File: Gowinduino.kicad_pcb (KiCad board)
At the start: 2 copper layers, 68.6 x 53.3 mm, 63 parts, among them J1 Power, J2 Analog, J3 Digital, J4 Digital, J5 SPI, J6 JTAG, J7 USB, J8 12V, SW1 Mode, SW2 Reset, U1 GW1NSR-4CQN48P, U2 W25Q32JVSS, U3 TXB0104PW, U4 MP2122, U5 FT2232HL, U6 93LC56B, U7 XC6206-3.3, U8 L7805, Y1 12M

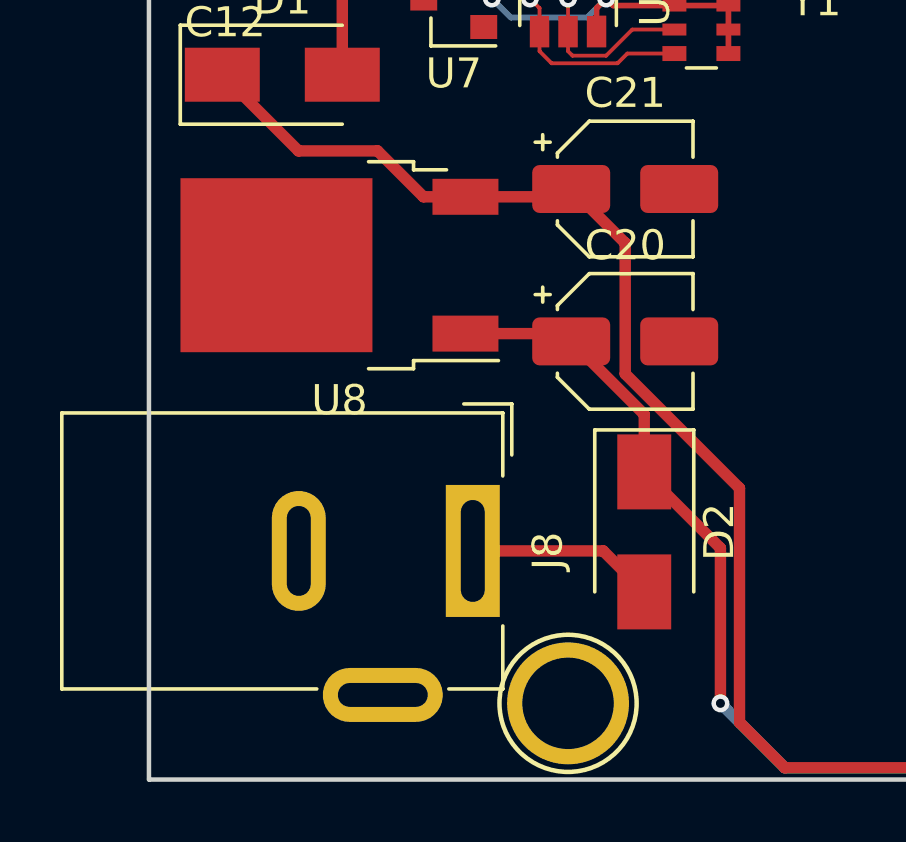
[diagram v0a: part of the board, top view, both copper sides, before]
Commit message: Via stitching at 5V regulator
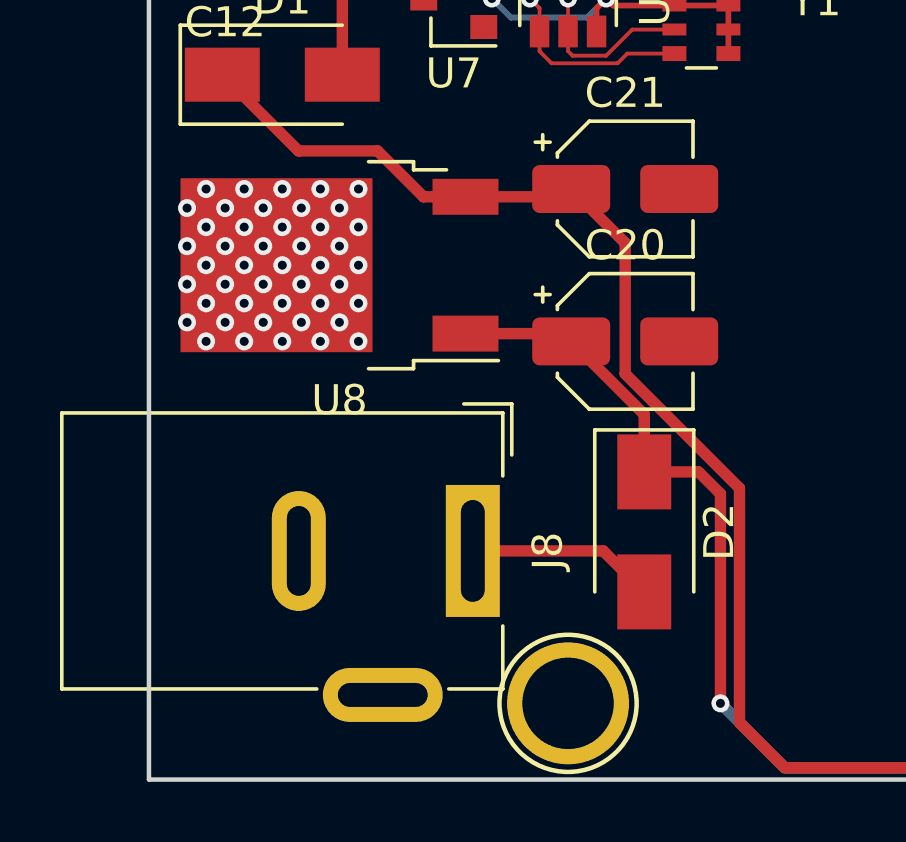
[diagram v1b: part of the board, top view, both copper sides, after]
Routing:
- net +12V: track 46.2 -> 47.3 mm
- net GND: vias 130 -> 175
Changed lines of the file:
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@@
     (thickness 1.6)
     (drawings 53)
-    (tracks 837)
+    (tracks 883)
     (zones 0)
     (modules 63)
@@
   (segment (start 151.454243 97.611827) (end 151.196056 97.35364) (width 0.127) (layer F.Cu) (net 0) (status 30))
   (segment (start 151.737086 97.328984) (end 151.478899 97.070797) (width 0.127) (layer F.Cu) (net 0) (status 30))
+  (via (at 117.983 111.76) (size 0.6) (drill 0.3) (layers F.Cu B.Cu) (net 2))
+  (via (at 117.983 106.68) (size 0.6) (drill 0.3) (layers F.Cu B.Cu) (net 2))
+  (via (at 112.903 111.76) (size 0.6) (drill 0.3) (layers F.Cu B.Cu) (net 2))
+  (via (at 112.268 111.125) (size 0.6) (drill 0.3) (layers F.Cu B.Cu) (net 2))
+  (via (at 116.713 106.68) (size 0.6) (drill 0.3) (layers F.Cu B.Cu) (net 2))
+  (via (at 117.348 107.315) (size 0.6) (drill 0.3) (layers F.Cu B.Cu) (net 2))
+  (via (at 117.983 107.95) (size 0.6) (drill 0.3) (layers F.Cu B.Cu) (net 2))
+  (via (at 116.078 109.855) (size 0.6) (drill 0.3) (layers F.Cu B.Cu) (net 2))
+  (via (at 114.173 111.76) (size 0.6) (drill 0.3) (layers F.Cu B.Cu) (net 2))
+  (via (at 113.538 111.125) (size 0.6) (drill 0.3) (layers F.Cu B.Cu) (net 2))
+  (via (at 112.903 110.49) (size 0.6) (drill 0.3) (layers F.Cu B.Cu) (net 2))
+  (via (at 112.268 109.855) (size 0.6) (drill 0.3) (layers F.Cu B.Cu) (net 2))
+  (via (at 115.443 106.68) (size 0.6) (drill 0.3) (layers F.Cu B.Cu) (net 2))
+  (via (at 116.078 107.315) (size 0.6) (drill 0.3) (layers F.Cu B.Cu) (net 2))
+  (via (at 116.713 107.95) (size 0.6) (drill 0.3) (layers F.Cu B.Cu) (net 2))
+  (via (at 117.348 108.585) (size 0.6) (drill 0.3) (layers F.Cu B.Cu) (net 2))
+  (via (at 117.983 109.22) (size 0.6) (drill 0.3) (layers F.Cu B.Cu) (net 2))
+  (via (at 116.713 110.49) (size 0.6) (drill 0.3) (layers F.Cu B.Cu) (net 2))
+  (via (at 115.443 111.76) (size 0.6) (drill 0.3) (layers F.Cu B.Cu) (net 2))
+  (via (at 114.808 111.125) (size 0.6) (drill 0.3) (layers F.Cu B.Cu) (net 2))
+  (via (at 114.173 110.49) (size 0.6) (drill 0.3) (layers F.Cu B.Cu) (net 2))
+  (via (at 113.538 109.855) (size 0.6) (drill 0.3) (layers F.Cu B.Cu) (net 2))
+  (via (at 112.903 109.22) (size 0.6) (drill 0.3) (layers F.Cu B.Cu) (net 2))
+  (via (at 112.268 108.585) (size 0.6) (drill 0.3) (layers F.Cu B.Cu) (net 2))
+  (via (at 114.173 106.68) (size 0.6) (drill 0.3) (layers F.Cu B.Cu) (net 2))
+  (via (at 114.808 107.315) (size 0.6) (drill 0.3) (layers F.Cu B.Cu) (net 2))
+  (via (at 115.443 107.95) (size 0.6) (drill 0.3) (layers F.Cu B.Cu) (net 2))
+  (via (at 116.078 108.585) (size 0.6) (drill 0.3) (layers F.Cu B.Cu) (net 2))
+  (via (at 116.713 109.22) (size 0.6) (drill 0.3) (layers F.Cu B.Cu) (net 2))
+  (via (at 117.348 109.855) (size 0.6) (drill 0.3) (layers F.Cu B.Cu) (net 2))
+  (via (at 117.983 110.49) (size 0.6) (drill 0.3) (layers F.Cu B.Cu) (net 2))
+  (via (at 117.348 111.125) (size 0.6) (drill 0.3) (layers F.Cu B.Cu) (net 2))
+  (via (at 116.713 111.76) (size 0.6) (drill 0.3) (layers F.Cu B.Cu) (net 2))
+  (via (at 116.078 111.125) (size 0.6) (drill 0.3) (layers F.Cu B.Cu) (net 2))
+  (via (at 115.443 110.49) (size 0.6) (drill 0.3) (layers F.Cu B.Cu) (net 2))
+  (via (at 114.808 109.855) (size 0.6) (drill 0.3) (layers F.Cu B.Cu) (net 2))
+  (via (at 114.173 109.22) (size 0.6) (drill 0.3) (layers F.Cu B.Cu) (net 2))
+  (via (at 113.538 108.585) (size 0.6) (drill 0.3) (layers F.Cu B.Cu) (net 2))
+  (via (at 112.903 107.95) (size 0.6) (drill 0.3) (layers F.Cu B.Cu) (net 2))
+  (via (at 112.268 107.315) (size 0.6) (drill 0.3) (layers F.Cu B.Cu) (net 2))
+  (via (at 112.903 106.68) (size 0.6) (drill 0.3) (layers F.Cu B.Cu) (net 2))
+  (via (at 113.538 107.315) (size 0.6) (drill 0.3) (layers F.Cu B.Cu) (net 2))
+  (via (at 114.173 107.95) (size 0.6) (drill 0.3) (layers F.Cu B.Cu) (net 2))
+  (via (at 114.808 108.585) (size 0.6) (drill 0.3) (layers F.Cu B.Cu) (net 2))
+  (via (at 115.443 109.22) (size 0.6) (drill 0.3) (layers F.Cu B.Cu) (net 2))
   (segment (start 177.038 95.885) (end 179.28074 98.12774) (width 0.1905) (layer B.Cu) (net 1))
   (segment (start 179.28074 113.165968) (end 174.498 117.948708) (width 0.1905) (layer B.Cu) (net 1))
@@
   (segment (start 132.19549 125.97249) (end 130.048 123.825) (width 0.381) (layer B.Cu) (net 42))
   (segment (start 154.57051 125.97249) (end 132.19549 125.97249) (width 0.381) (layer B.Cu) (net 42))
-  (segment (start 130.048 118.65) (end 127.508 116.11) (width 0.381) (layer F.Cu) (net 42))
-  (segment (start 130.048 123.825) (end 130.048 118.65) (width 0.381) (layer F.Cu) (net 42))
+  (segment (start 129.318 116.11) (end 127.508 116.11) (width 0.381) (layer F.Cu) (net 42))
+  (segment (start 130.048 116.84) (end 129.318 116.11) (width 0.381) (layer F.Cu) (net 42))
+  (segment (start 130.048 123.825) (end 130.048 116.84) (width 0.381) (layer F.Cu) (net 42))
   (segment (start 154.163 88.25) (end 154.178 88.265) (width 0.127) (layer F.Cu) (net 43))
   (segment (start 150.0555 88.25) (end 154.163 88.25) (width 0.127) (layer F.Cu) (net 43) (status 10))
